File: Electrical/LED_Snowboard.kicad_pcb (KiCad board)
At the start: 2 copper layers, 69 parts, among them CON1 BARREL_JACK, P1 CONN_01X02, P2 CONN_01X05, P3 CONN_01X03, P4 CONN_01X03, U2 TPS63021, U3 TPS61236, U4 BQ24170, U5 LSM9DS1, U7 SN74AHCT125

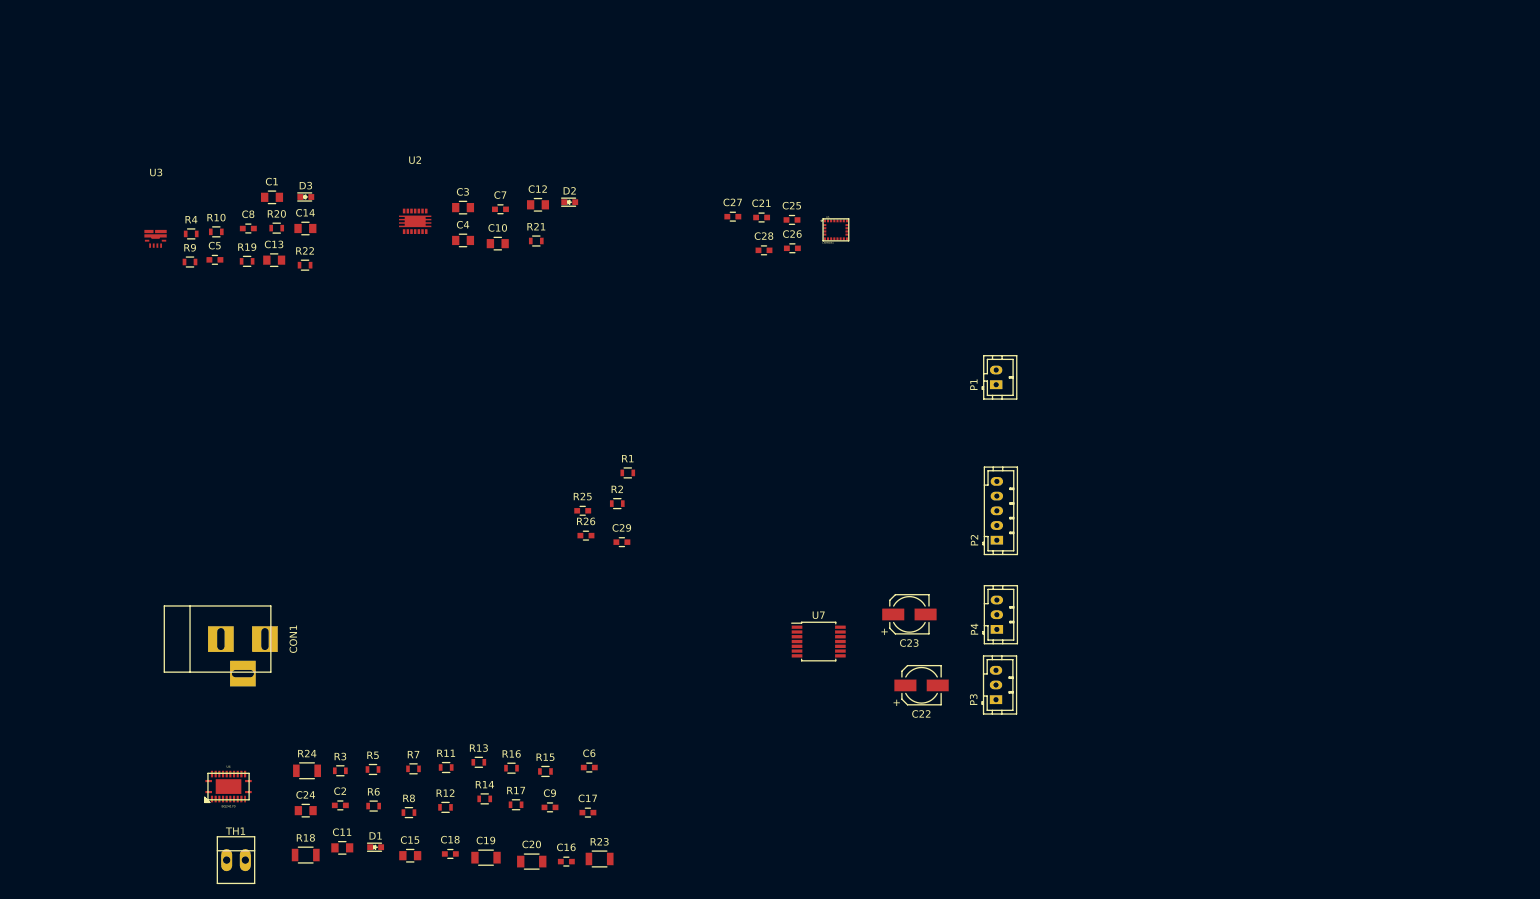
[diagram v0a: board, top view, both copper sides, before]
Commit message: PCB work continuing, all footprints finished
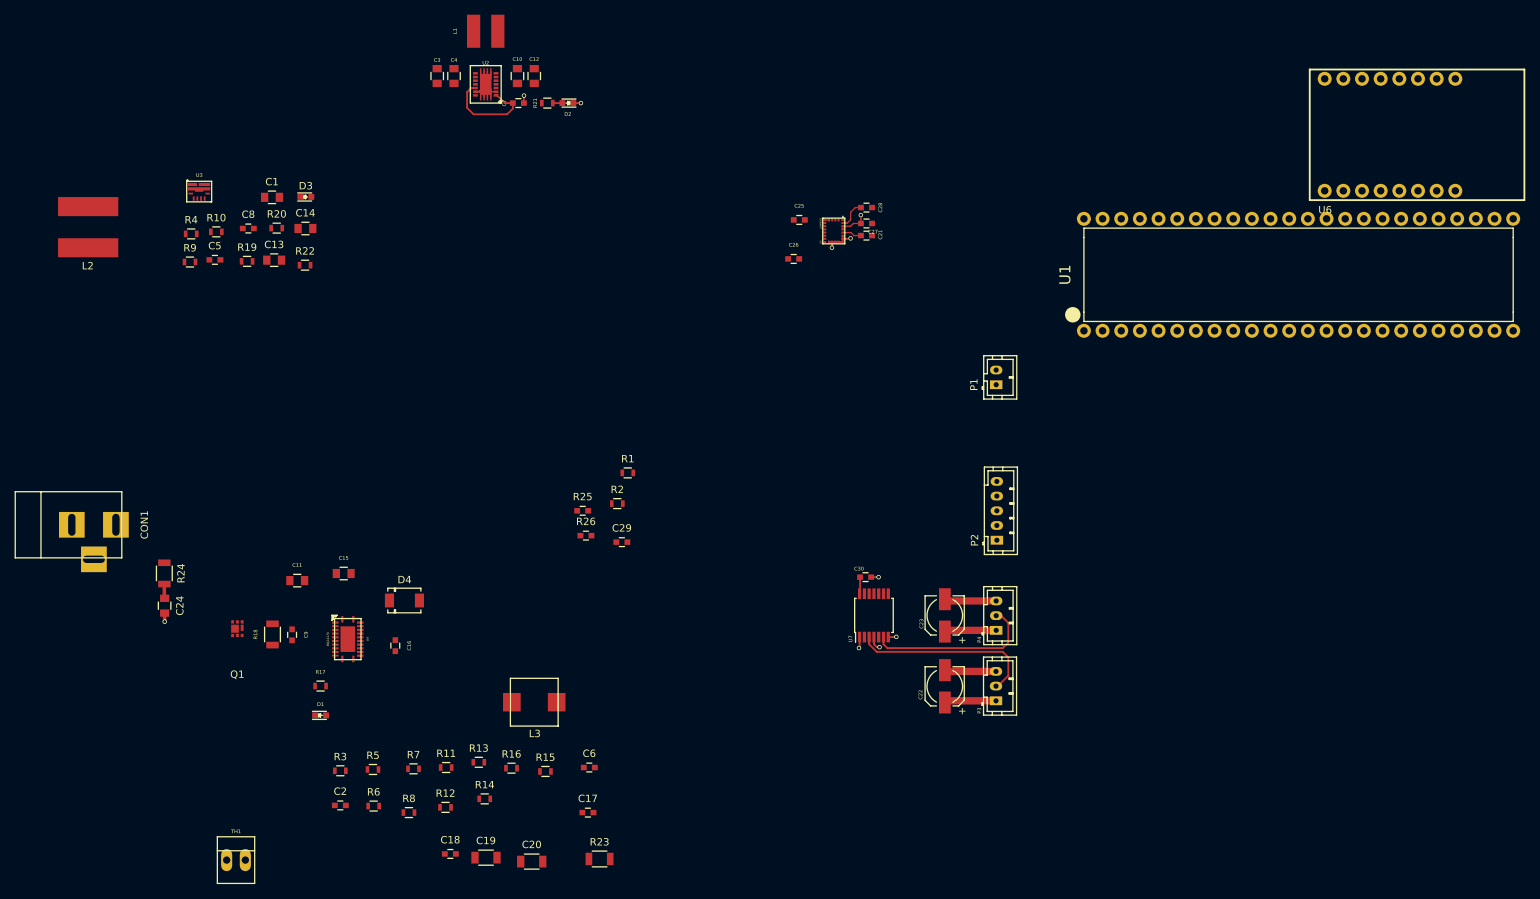
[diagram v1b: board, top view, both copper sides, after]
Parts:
- added C30: 1uF, Capacitors_SMD:C_0603, F.Cu at (184.0, 95.0)
- added D4: FSV530AF, Snow_parts:DO-214AD, F.Cu at (121.3, 98.2)
- added L1: 1.4uH, Snow_parts:SDR0403-1R4ML, F.Cu at (132.3, 20.7)
- added L2: 1uH, Snow_parts:SRN8040-1R0Y, F.Cu at (78.2, 47.4)
- added L3: 3.3uH, Snow_parts:SRP7030-3R3FM, F.Cu at (138.9, 112.0)
- added Q1: CSD17313Q2, Snow_parts:WSON-FET-6, F.Cu at (98.5, 102.0)
- added U1: Teensy_3.6, Snow_parts:Teensy-3.6, F.Cu at (216.3, 61.5)
- added U6: VenusGPS, Snow_parts:VenusGPS, F.Cu at (246.5, 42.4)
- R21: value R -> 260
- R22: value R -> 600
- moved C9 42.2 mm to (106.0, 102.8), turned to 270 degrees
- moved C15 39.5 mm to (113.0, 94.5)
- moved C16 37.5 mm to (120.0, 104.3), turned to 270 degrees
- moved C11 36.9 mm to (106.7, 95.5)
- moved C24 33.9 mm to (88.6, 98.9), turned to 270 degrees
- moved R24 33.1 mm to (88.6, 94.5), turned to 270 degrees
- moved R17 31.1 mm to (109.9, 109.8)
- moved R18 30.4 mm to (103.3, 102.8), turned to 90 degrees
- moved U4 25.8 mm to (113.6, 103.4), turned to 270 degrees
- moved CON1 25.6 mm to (75.8, 87.9)
- moved C10 23.0 mm to (136.7, 26.8), turned to 90 degrees
- moved C4 22.4 mm to (128.0, 26.8), turned to 90 degrees
- moved U2 21.0 mm to (132.3, 27.9), turned to 90 degrees
- moved D1 19.4 mm to (109.9, 113.8)
- moved R21 18.8 mm to (140.7, 30.5)
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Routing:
- net GND: track 0.00 -> 48.2 mm, vias 0 -> 9
- net /Connectors/LED_out1: track 0.00 -> 25.4 mm
- net /Connectors/LED_out2: track 0.00 -> 23.2 mm
- net +5V: track 0.00 -> 16.4 mm
- net Net-(C7-Pad1): track 0.00 -> 13.9 mm
- net +3V3: track 0.00 -> 4.21 mm, vias 0 -> 1
- net Net-(C28-Pad1): track 0.00 -> 3.94 mm
- net Net-(C21-Pad1): track 0.00 -> 2.65 mm
- net Net-(C24-Pad1): track 0.00 -> 1.96 mm
- net Net-(D2-Pad2): track 0.00 -> 1.29 mm
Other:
- rule trace_min: 0.2 -> 0.14

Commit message: PCB 90% done
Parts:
- P1: footprint Connectors_JST:JST_PH_B2B-PH-K_02x2.00mm_Straight -> Connect:PINHEAD1-2
- moved U6 146.5 mm to (107.7, 89.1), turned to 90 degrees
- moved P1 92.1 mm to (123.1, 116.6), turned to 180 degrees
- moved U3 83.0 mm to (137.2, 112.8), turned to 270 degrees
- moved D3 81.6 mm to (143.3, 116.8), turned to 90 degrees
- moved R4 81.4 mm to (137.4, 116.0), turned to 180 degrees
- moved L2 80.4 mm to (134.5, 104.7), turned to 90 degrees
- moved R9 79.8 mm to (137.4, 117.8)
- moved C8 77.6 mm to (133.0, 117.8), turned to 90 degrees
- moved C29 75.7 mm to (221.2, 62.1)
- moved R25 75.7 mm to (215.8, 57.8)
- moved R26 75.7 mm to (216.3, 61.2)
- moved R10 74.7 mm to (133.1, 112.6), turned to 270 degrees
- moved R19 74.4 mm to (134.6, 117.8), turned to 90 degrees
- moved R20 74.3 mm to (133.9, 115.5), turned to 180 degrees
- moved C14 73.8 mm to (142.4, 112.7), turned to 90 degrees
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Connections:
- C1 pad 1: /Power Supply/V_SYS -> /BAT
- C13 pad 1: /5V -> +5V
- C14 pad 1: /5V -> +5V
- C18 pad 2: /Power Supply/V_SYS -> Net-(C18-Pad2)
- C3 pad 1: /Power Supply/V_SYS -> /BAT
- C4 pad 1: /Power Supply/V_SYS -> /BAT
- C8 pad 1: /5V -> +5V
- CON1 pad 1: +12V -> /V_IN_Conn
- L2 pad 1: /Power Supply/V_SYS -> /BAT
- L3 pad 2: /Power Supply/V_SYS -> Net-(C18-Pad2)
- P1 pad 1: +BATT -> /BAT
- R19 pad 1: /5V -> +5V
- R22 pad 1: /5V -> +5V
- R23 pad 2: /Power Supply/V_SYS -> Net-(C18-Pad2)
- R4 pad 2: /Power Supply/V_SYS -> /BAT
- R9 pad 1: /Power Supply/V_SYS -> /BAT
- U2 pad 10: /Power Supply/V_SYS -> /BAT
- U2 pad 11: /Power Supply/V_SYS -> /BAT
- U3 pad 3: /Power Supply/V_SYS -> /BAT
- U3 pad 7: /Power Supply/V_SYS -> /BAT
- U3 pad 9: /5V -> +5V
- U4 pad 16: /Power Supply/V_SYS -> Net-(C18-Pad2)
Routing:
- net /BAT: track 0.00 -> 85.2 mm, vias 0 -> 2
- net /UART_RX_TX: track 0.00 -> 83.3 mm
- net /UART_TX_RX: track 0.00 -> 79.7 mm
- net GND: track 48.2 -> 122.6 mm, vias 9 -> 51
- net +5V: track 16.4 -> 83.7 mm
- net /LED_CTRL_Conn: track 0.00 -> 33.5 mm
- net /I2C_SDA_Conn: track 0.00 -> 29.8 mm, vias 0 -> 1
- net /I2C_SCL_Conn: track 0.00 -> 27.3 mm, vias 0 -> 1
- net /DISP_RST_Conn: track 0.00 -> 25.0 mm
- net /Power Supply/VREF: track 0.00 -> 18.6 mm, vias 0 -> 2
- net /Power Supply/TS: track 0.00 -> 18.0 mm, vias 0 -> 2
- net /Power Supply/OVPSET: track 0.00 -> 18.0 mm, vias 0 -> 2
- net /V_IN_Conn: track 0.00 -> 16.6 mm
- net Net-(C18-Pad2): track 0.00 -> 15.4 mm
- net Net-(C11-Pad1): track 0.00 -> 14.5 mm
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- added copper zone on F.Cu, net +5V
- added copper zone on F.Cu, net /3.3V
- added copper zone on F.Cu, net /BAT
- added copper zone on F.Cu, net /V_IN_Conn
- added copper zone on B.Cu, net GND
- added copper zone on F.Cu, net GND
- added copper zone on F.Cu, net Net-(C11-Pad1)
- added copper zone on F.Cu, net Net-(C17-Pad1)
- added copper zone on F.Cu, net Net-(C18-Pad2)
- added copper zone on F.Cu, net Net-(C9-Pad2)
- added copper zone on F.Cu, net Net-(L1-Pad1)
- added copper zone on F.Cu, net Net-(L1-Pad2)
- added copper zone on F.Cu, net Net-(L2-Pad2)
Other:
- board outline added: 85 x 60 mm

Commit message: Finished PCB
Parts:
- added REF**: MountingHole_3.2mm_M3, Mounting_Holes:MountingHole_3.2mm_M3, F.Cu at (172.0, 69.0)
- added REF**: MountingHole_3.2mm_M3, Mounting_Holes:MountingHole_3.2mm_M3, F.Cu at (94.0, 64.1)
- added REF**: MountingHole_3.2mm_M3, Mounting_Holes:MountingHole_3.2mm_M3, F.Cu at (94.0, 117.0)
- added REF**: MountingHole_3.2mm_M3, Mounting_Holes:MountingHole_3.2mm_M3, F.Cu at (172.0, 117.0)
- moved C29 87.5 mm to (139.6, 93.6), turned to 180 degrees
- moved R25 85.6 mm to (139.6, 96.8)
- moved R26 83.9 mm to (139.6, 95.2), turned to 180 degrees
- moved R1 40.8 mm to (149.5, 76.1), turned to 270 degrees
- moved R2 37.7 mm to (152.1, 76.1), turned to 270 degrees
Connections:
- C10 pad 1: /3.3V -> +3V3
- C12 pad 1: /3.3V -> +3V3
- R21 pad 1: /3.3V -> +3V3
- R25 pad 1: /BAT_V -> /BAT
- U2 pad 3: /3.3V -> +3V3
- U2 pad 4: /3.3V -> +3V3
- U2 pad 5: /3.3V -> +3V3
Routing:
- net +3V3: track 11.7 -> 162.9 mm, vias 3 -> 5
- net GND: track 122.6 -> 223.8 mm, vias 51 -> 86
- net /Microcontroller/BAT_MON: track 0.00 -> 20.2 mm
- net /3.3V: track 11.8 -> 0.00 mm
- net /BAT: track 85.2 -> 88.8 mm
- net /I2C_SCL_Conn: track 27.3 -> 29.4 mm
- net /I2C_SDA_Conn: track 29.8 -> 31.9 mm
- net (no net): vias 1 -> 0
- added copper zone on F.Cu, net +3V3
- removed copper zone on F.Cu, net /3.3V
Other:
- board text added: "LED Snowboard Project Rev 1 GIS 12/2016"

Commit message: Minor Changes
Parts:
- C29: value C -> 1uF
- R25: value R -> 10K
- R26: value R -> 36K
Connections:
- U4 pad 25: (no net) -> GND
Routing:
- net GND: track 223.8 -> 268.5 mm, vias 86 -> 109
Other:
- board text added: "-+"
- board text added: "3.3V SDA SCL RST GND"
- board text added: "5V CTRL GND"
